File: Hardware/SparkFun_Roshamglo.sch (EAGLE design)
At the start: 42 parts, among them IC1 ATTINY84A, J1 R_Ext, J2 USBPCB, Q1 600mA/40V, U1 IR-Receiver, U3 AP2112K-3.3V

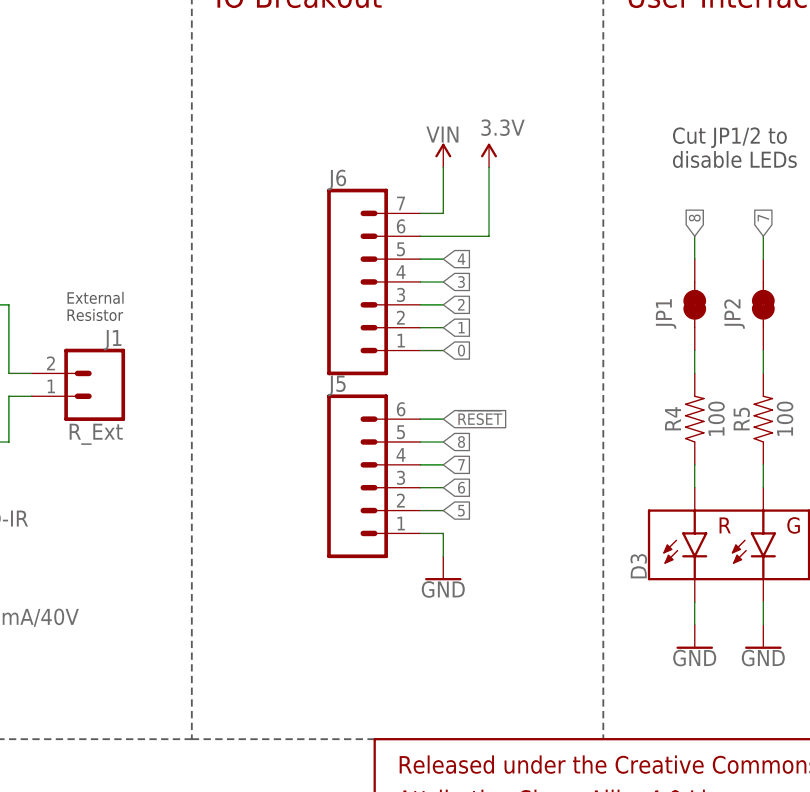
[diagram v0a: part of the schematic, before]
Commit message: v02 changes
- Switch back to old size for lanyard clip
- Changed the "@" to proportional
- Moved pin 4 to other header to leave more room for battery terminal
soldering
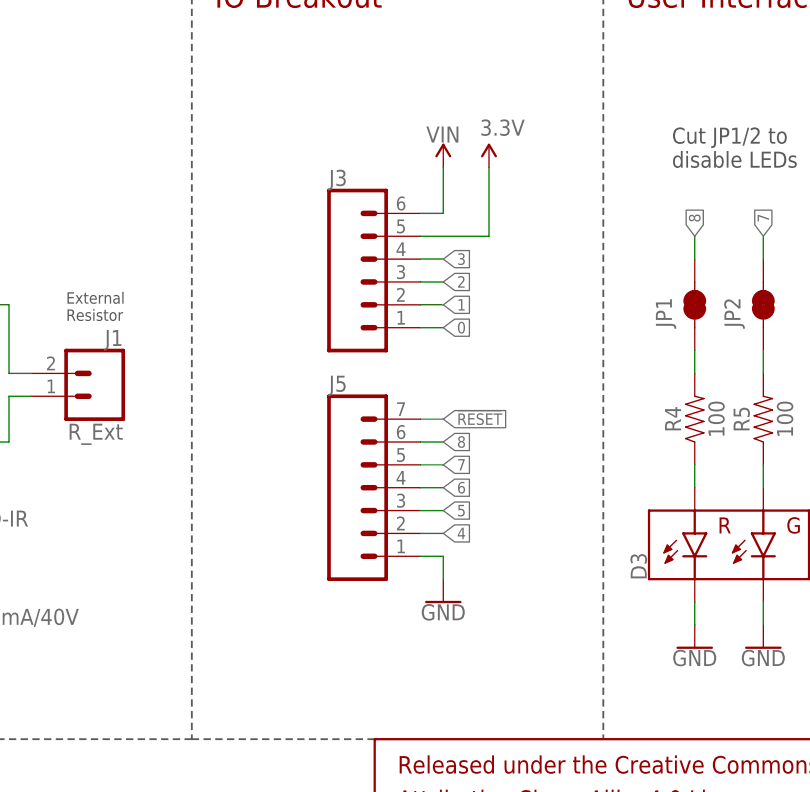
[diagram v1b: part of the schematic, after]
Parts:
- removed J6: (no value), SparkFun-Connectors:CONN_07NO_SILK
- added J3: (no value), SparkFun-Connectors:CONN_06NO_SILK_FEMALE_PTH
- J5: device SparkFun-Connectors:CONN_06NO_SILK_FEMALE_PTH -> SparkFun-Connectors:CONN_07NO_SILK
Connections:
- net !RESET: now also J5.7; no longer J5.6
- net 0: now also J3.1; no longer J6.1
- net 1: now also J3.2; no longer J6.2
- net 2: now also J3.3; no longer J6.3
- net 3: now also J3.4; no longer J6.4
- net 3.3V: now also J3.5; no longer J6.6
- net 4: now also J5.2; no longer J6.5
- net 5: now also J5.3; no longer J5.2
- net 6: now also J5.4; no longer J5.3
- net 7: now also J5.5; no longer J5.4
- net 8: now also J5.6; no longer J5.5
- net VIN: now also J3.6; no longer J6.7
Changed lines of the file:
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@@
 <part name="GND11" library="SparkFun-Aesthetics" deviceset="GND" device=""/>
 <part name="SUPPLY7" library="SparkFun-Aesthetics" deviceset="3.3V" device=""/>
-<part name="J5" library="SparkFun-Connectors" deviceset="CONN_06" device="NO_SILK_FEMALE_PTH"/>
-<part name="J6" library="SparkFun-Connectors" deviceset="CONN_07" device="NO_SILK"/>
+<part name="J5" library="SparkFun-Connectors" deviceset="CONN_07" device="NO_SILK"/>
 <part name="GND9" library="SparkFun-PowerSymbols" deviceset="GND" device=""/>
 <part name="SUPPLY8" library="SparkFun-PowerSymbols" deviceset="VIN" device=""/>
@@
 <part name="SUPPLY2" library="SparkFun-Aesthetics" deviceset="3.3V" device=""/>
 <part name="JP5" library="SparkFun-Jumpers" deviceset="JUMPER-SMT_2_NC_TRACE" device="_SILK" value=""/>
+<part name="J3" library="SparkFun-Connectors" deviceset="CONN_06" device="NO_SILK_FEMALE_PTH"/>
 </parts>
 <sheets>
@@
 <instance part="GND11" gate="1" x="99.06" y="40.64"/>
 <instance part="SUPPLY7" gate="G$1" x="99.06" y="86.36"/>
-<instance part="J5" gate="G$1" x="147.32" y="63.5"/>
-<instance part="J6" gate="G$1" x="147.32" y="83.82"/>
-<instance part="GND9" gate="1" x="154.94" y="53.34"/>
+<instance part="J5" gate="G$1" x="147.32" y="60.96"/>
+<instance part="GND9" gate="1" x="154.94" y="50.8"/>
 <instance part="SUPPLY8" gate="G$1" x="154.94" y="99.06"/>
 <instance part="SUPPLY10" gate="G$1" x="160.02" y="99.06"/>
@@
 <instance part="SUPPLY2" gate="G$1" x="104.14" y="167.64"/>
 <instance part="JP5" gate="G$1" x="104.14" y="160.02" rot="R270"/>
+<instance part="J3" gate="G$1" x="147.32" y="86.36"/>
 </instances>
 <busses>
@@
 </segment>
 <segment>
-<pinref part="J6" gate="G$1" pin="6"/>
-<wire x1="152.4" y1="91.44" x2="160.02" y2="91.44" width="0.1524" layer="91"/>
 <pinref part="SUPPLY10" gate="G$1" pin="3.3V"/>
 <wire x1="160.02" y1="91.44" x2="160.02" y2="99.06" width="0.1524" layer="91"/>
+<pinref part="J3" gate="G$1" pin="5"/>
+<wire x1="152.4" y1="91.44" x2="160.02" y2="91.44" width="0.1524" layer="91"/>
 </segment>
 <segment>
@@
 <segment>
 <pinref part="J5" gate="G$1" pin="1"/>
-<wire x1="152.4" y1="58.42" x2="154.94" y2="58.42" width="0.1524" layer="91"/>
-<wire x1="154.94" y1="58.42" x2="154.94" y2="55.88" width="0.1524" layer="91"/>
+<wire x1="152.4" y1="55.88" x2="154.94" y2="55.88" width="0.1524" layer="91"/>
+<wire x1="154.94" y1="55.88" x2="154.94" y2="53.34" width="0.1524" layer="91"/>
 <pinref part="GND9" gate="1" pin="GND"/>
 </segment>
@@
 </segment>
 <segment>
-<pinref part="J5" gate="G$1" pin="6"/>
+<label x="154.94" y="71.12" size="1.27" layer="95" xref="yes"/>
+<pinref part="J5" gate="G$1" pin="7"/>
 <wire x1="152.4" y1="71.12" x2="154.94" y2="71.12" width="0.1524" layer="91"/>
-<label x="154.94" y="71.12" size="1.27" layer="95" xref="yes"/>
 </segment>
 </net>
@@
 </segment>
 <segment>
-<pinref part="J5" gate="G$1" pin="5"/>
+<label x="154.94" y="68.58" size="1.27" layer="95" xref="yes"/>
+<pinref part="J5" gate="G$1" pin="6"/>
 <wire x1="152.4" y1="68.58" x2="154.94" y2="68.58" width="0.1524" layer="91"/>
-<label x="154.94" y="68.58" size="1.27" layer="95" xref="yes"/>
 </segment>
 <segment>
@@
 </segment>
 <segment>
-<pinref part="J5" gate="G$1" pin="4"/>
-<wire x1="152.4" y1="66.04" x2="154.94" y2="66.04" width="0.1524" layer="91"/>
-<label x="154.94" y="66.04" size="1.27" layer="95" xref="yes"/>
-</segment>
-<segment>
 <pinref part="JP2" gate="G$1" pin="2"/>
 <wire x1="190.5" y1="88.9" x2="190.5" y2="91.44" width="0.1524" layer="91"/>
 <label x="190.5" y="91.44" size="1.27" layer="95" rot="R90" xref="yes"/>
 </segment>
+<segment>
+<pinref part="J5" gate="G$1" pin="5"/>
+<wire x1="152.4" y1="66.04" x2="154.94" y2="66.04" width="0.1524" layer="91"/>
+<label x="154.94" y="66.04" size="1.27" layer="95" xref="yes"/>
+</segment>
 </net>
 <net name="6" class="0">
@@
 </segment>
 <segment>
-<pinref part="J5" gate="G$1" pin="3"/>
-<wire x1="152.4" y1="63.5" x2="154.94" y2="63.5" width="0.1524" layer="91"/>
-<label x="154.94" y="63.5" size="1.27" layer="95" xref="yes"/>
-</segment>
-<segment>
 <pinref part="S1" gate="G$1" pin="CENT"/>
 <wire x1="236.22" y1="88.9" x2="238.76" y2="88.9" width="0.1524" layer="91"/>
 <label x="238.76" y="88.9" size="1.27" layer="95" xref="yes"/>
 </segment>
+<segment>
+<pinref part="J5" gate="G$1" pin="4"/>
+<wire x1="152.4" y1="63.5" x2="154.94" y2="63.5" width="0.1524" layer="91"/>
+<label x="154.94" y="63.5" size="1.27" layer="95" xref="yes"/>
+</segment>
 </net>
 <net name="5" class="0">
@@
 </segment>
 <segment>
-<pinref part="J5" gate="G$1" pin="2"/>
-<wire x1="152.4" y1="60.96" x2="154.94" y2="60.96" width="0.1524" layer="91"/>
-<label x="154.94" y="60.96" size="1.27" layer="95" xref="yes"/>
-</segment>
-<segment>
 <pinref part="JP3" gate="G$1" pin="2"/>
 <wire x1="68.58" y1="50.8" x2="66.04" y2="50.8" width="0.1524" layer="91"/>
 <label x="66.04" y="50.8" size="1.27" layer="95" rot="R180" xref="yes"/>
 </segment>
+<segment>
+<pinref part="J5" gate="G$1" pin="3"/>
+<wire x1="152.4" y1="60.96" x2="154.94" y2="60.96" width="0.1524" layer="91"/>
+<label x="154.94" y="60.96" size="1.27" layer="95" xref="yes"/>
+</segment>
 </net>
 <net name="4" class="0">
@@
 </segment>
 <segment>
-<label x="154.94" y="88.9" size="1.27" layer="95" xref="yes"/>
-<pinref part="J6" gate="G$1" pin="5"/>
-<wire x1="152.4" y1="88.9" x2="154.94" y2="88.9" width="0.1524" layer="91"/>
+<pinref part="J5" gate="G$1" pin="2"/>
+<wire x1="152.4" y1="58.42" x2="154.94" y2="58.42" width="0.1524" layer="91"/>
+<label x="154.94" y="58.42" size="1.27" layer="95" xref="yes"/>
 </segment>
 </net>
@@
 </segment>
 <segment>
-<label x="154.94" y="86.36" size="1.27" layer="95" xref="yes"/>
-<pinref part="J6" gate="G$1" pin="4"/>
-<wire x1="152.4" y1="86.36" x2="154.94" y2="86.36" width="0.1524" layer="91"/>
+<label x="154.94" y="88.9" size="1.27" layer="95" xref="yes"/>
+<pinref part="J3" gate="G$1" pin="4"/>
+<wire x1="152.4" y1="88.9" x2="154.94" y2="88.9" width="0.1524" layer="91"/>
 </segment>
 <segment>
@@
 </segment>
 <segment>
-<label x="154.94" y="83.82" size="1.27" layer="95" xref="yes"/>
-<pinref part="J6" gate="G$1" pin="3"/>
-<wire x1="152.4" y1="83.82" x2="154.94" y2="83.82" width="0.1524" layer="91"/>
+<label x="154.94" y="86.36" size="1.27" layer="95" xref="yes"/>
+<pinref part="J3" gate="G$1" pin="3"/>
+<wire x1="152.4" y1="86.36" x2="154.94" y2="86.36" width="0.1524" layer="91"/>
 </segment>
 </net>
@@
 </segment>
 <segment>
-<label x="154.94" y="81.28" size="1.27" layer="95" xref="yes"/>
-<pinref part="J6" gate="G$1" pin="2"/>
-<wire x1="152.4" y1="81.28" x2="154.94" y2="81.28" width="0.1524" layer="91"/>
+<label x="154.94" y="83.82" size="1.27" layer="95" xref="yes"/>
+<pinref part="J3" gate="G$1" pin="2"/>
+<wire x1="152.4" y1="83.82" x2="154.94" y2="83.82" width="0.1524" layer="91"/>
 </segment>
 </net>
@@
 </segment>
 <segment>
-<label x="154.94" y="78.74" size="1.27" layer="95" xref="yes"/>
-<pinref part="J6" gate="G$1" pin="1"/>
-<wire x1="152.4" y1="78.74" x2="154.94" y2="78.74" width="0.1524" layer="91"/>
+<label x="154.94" y="81.28" size="1.27" layer="95" xref="yes"/>
+<pinref part="J3" gate="G$1" pin="1"/>
+<wire x1="152.4" y1="81.28" x2="154.94" y2="81.28" width="0.1524" layer="91"/>
 </segment>
 </net>
@@
 </segment>
 <segment>
-<pinref part="J6" gate="G$1" pin="7"/>
-<wire x1="152.4" y1="93.98" x2="154.94" y2="93.98" width="0.1524" layer="91"/>
 <pinref part="SUPPLY8" gate="G$1" pin="VIN"/>
 <wire x1="154.94" y1="93.98" x2="154.94" y2="99.06" width="0.1524" layer="91"/>
-</segment>
-</net>
+<pinref part="J3" gate="G$1" pin="6"/>
+<wire x1="152.4" y1="93.98" x2="154.94" y2="93.98" width="0.1524" layer="91"/>
+</segment>
+</net>

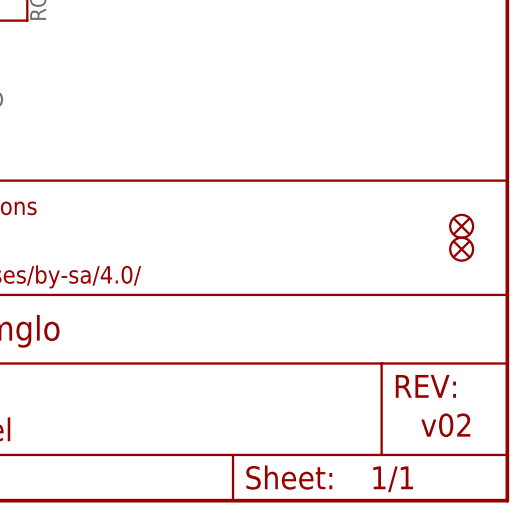
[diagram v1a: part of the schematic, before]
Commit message: Minor fixes
Added ordering instructions to bottom of board
Removed right angles in traces
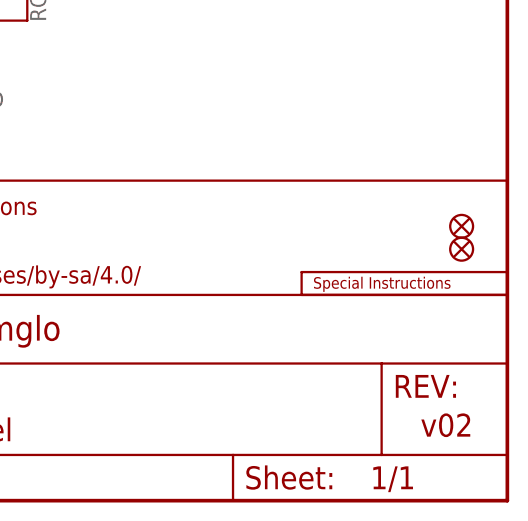
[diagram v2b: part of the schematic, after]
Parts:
- added U$5: SPECIAL_INSTRUCTIONS-ORDERING, SparkFun-Aesthetics:SPECIAL_INSTRUCTIONS-ORDERING
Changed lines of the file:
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@@
 <part name="JP5" library="SparkFun-Jumpers" deviceset="JUMPER-SMT_2_NC_TRACE" device="_SILK" value=""/>
 <part name="J3" library="SparkFun-Connectors" deviceset="CONN_06" device="NO_SILK_FEMALE_PTH"/>
+<part name="U$5" library="SparkFun-Aesthetics" deviceset="SPECIAL_INSTRUCTIONS" device="-ORDERING"/>
 </parts>
 <sheets>
@@
 <instance part="JP5" gate="G$1" x="104.14" y="160.02" rot="R270"/>
 <instance part="J3" gate="G$1" x="147.32" y="86.36"/>
+<instance part="U$5" gate="G$1" x="226.06" y="22.86"/>
 </instances>
 <busses>

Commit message: V10 changes
- Removed zener diodes
- Changed 33ohm IR LED resistor to 2.55k
- Removed paste on USB conn
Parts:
- removed D1, D2: 3.3V, SparkFun-DiscreteSemi:DIODE-ZENER-MM3Z3V3T1G
- J2: device SparkFun-Connectors:USBPCB -> SparkFun-Connectors:USBPCB_NOPASTE
- R6: value 33 -> 2.55k; device SparkFun-Resistors:33OHM-0603-1/10W-1% -> SparkFun-Resistors:2.55KOHM-0603-1/10W-1%
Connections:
- net D+: no longer D2.C
- net D-: no longer D1.C
- net GND: no longer D1.A, D2.A
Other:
- note added: "External Resistor 25 Ohm (min)"
- note removed: "External Resistor"
- moved on the sheet: JP4, U1
